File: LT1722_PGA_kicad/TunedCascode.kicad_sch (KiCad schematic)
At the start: 10 parts, among them U1 LT1722

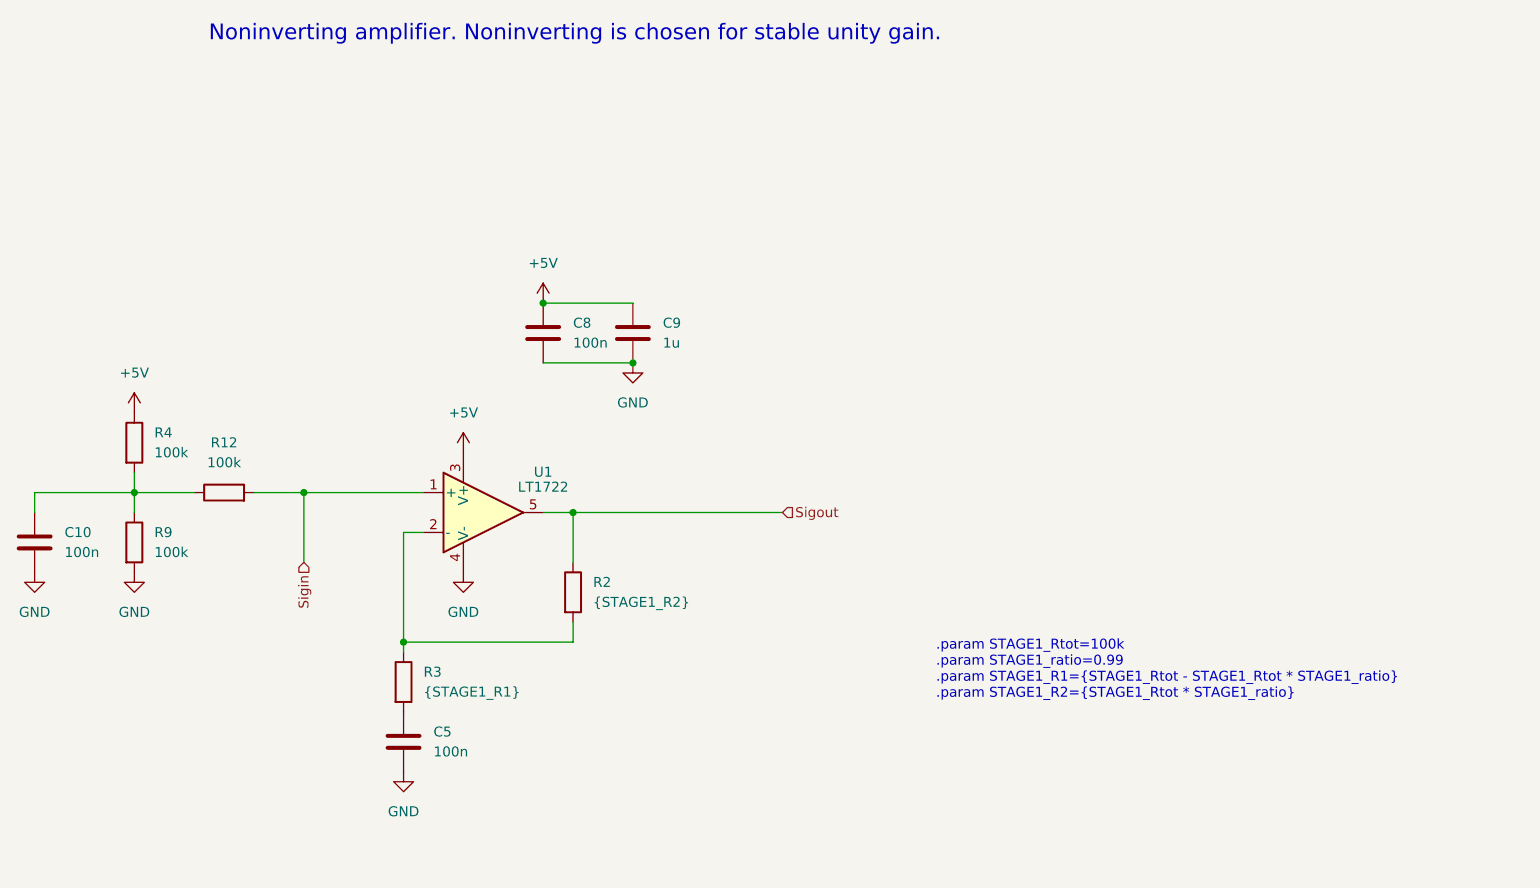
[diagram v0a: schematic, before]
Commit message: change to bypass of first stage amplifier, add schematic for a tuned cascode
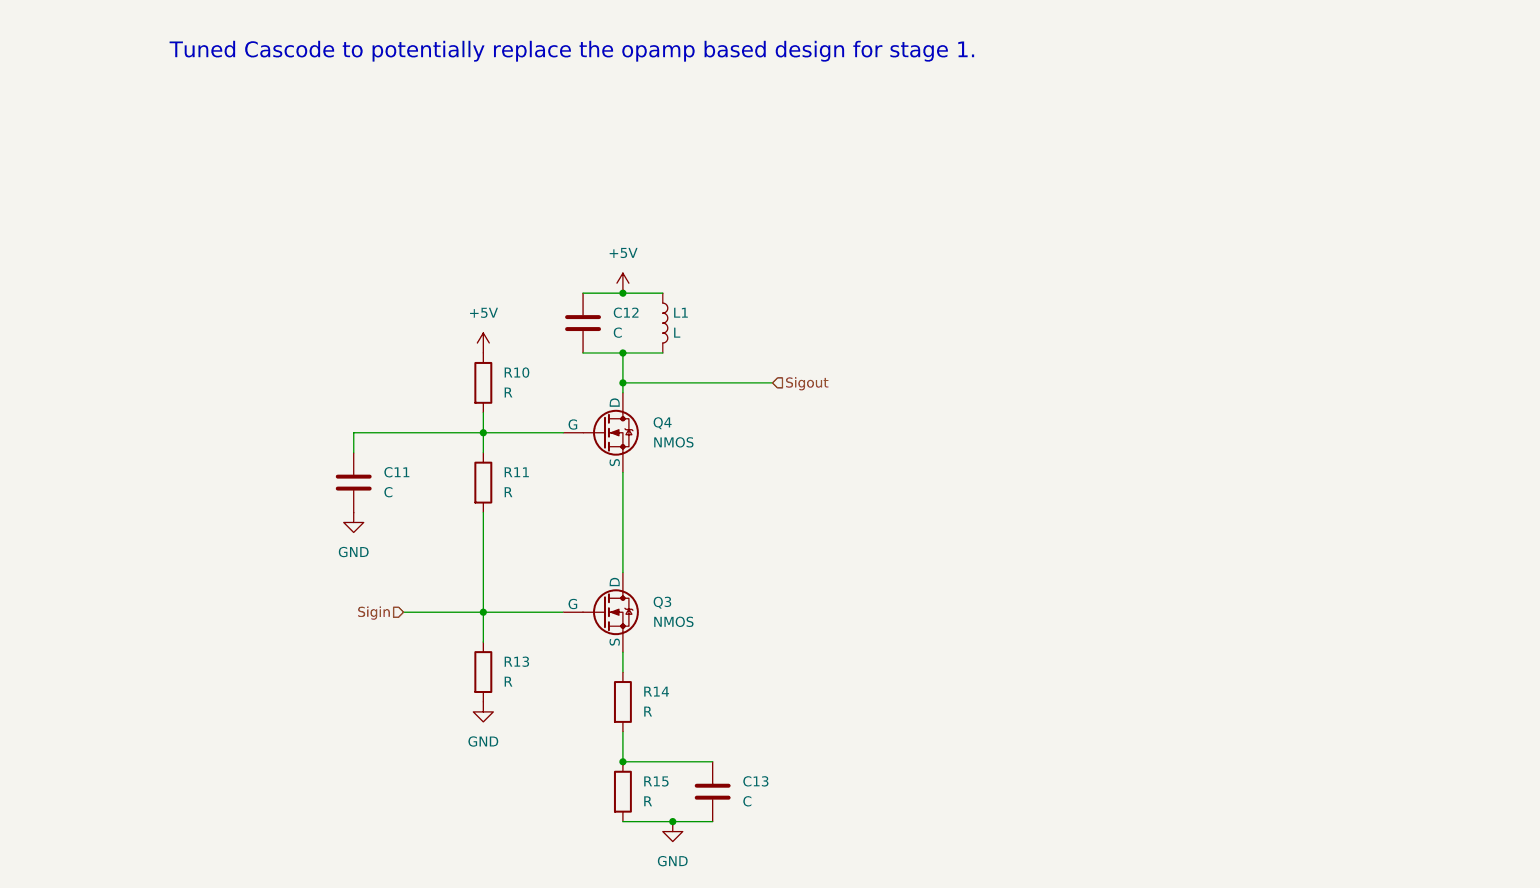
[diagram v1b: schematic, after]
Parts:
- removed C10, C5, C8: 100n, symbol Device:C
- removed C9: 1u, symbol Device:C
- removed R12, R4, R9: 100k, symbol Device:R
- removed R2: {STAGE1_R2}, symbol Device:R
- removed R3: {STAGE1_R1}, symbol Device:R
- removed U1: LT1722, symbol Simulation_SPICE:OPAMP
- added C11, C12, C13: C, symbol Device:C
- added L1: L, symbol Device:L
- added Q3, Q4: NMOS, symbol Simulation_SPICE:NMOS
- added R10, R11, R13, R14, R15: R, symbol Device:R
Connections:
- net +5V: now also C12.1, L1.1, R10.1
- net GND: now also C11.2, C13.2, R13.2, R15.2
- net Sigin: now also Q3.2 (G), R11.2, R13.1
- net Sigout: now also C12.2, L1.2, Q4.1 (D)
- new net: Q3.1 (D), Q4.3 (S)
- new net: Q3.3 (S), R14.1
- new net: C11.1, Q4.2 (G), R10.2, R11.1
- new net: C13.1, R14.2, R15.1
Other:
- note added: "Tuned Cascode to potentially replace the opamp based design for stage 1."
- note removed: ".param STAGE1_Rtot=100k .param STAGE1_ratio=0.99 .param STAGE1_R1={STAGE1_Rtot - STAGE1_Rtot * STAGE1_ratio} .param STAGE1_R2={STAGE1_Rtot * STAGE1_ratio}"
- note removed: "Noninverting amplifier. Noninverting is chosen for stable unity gain."
